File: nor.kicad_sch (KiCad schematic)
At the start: 4 parts, among them Q10 2N7002, Q11 DMP3099L, Q12 DMP3099L, Q9 2N7002

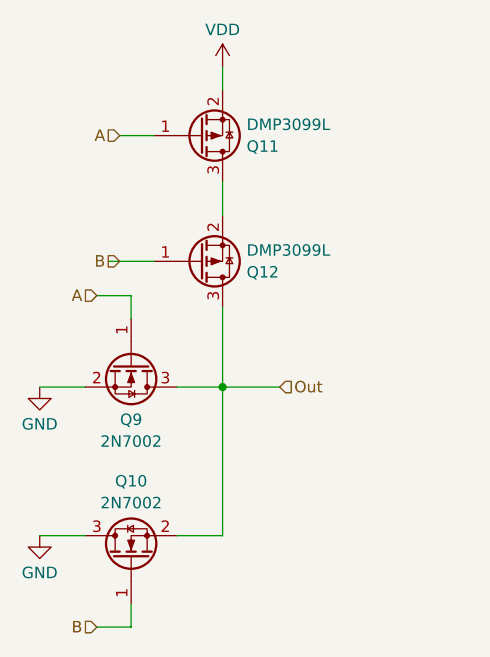
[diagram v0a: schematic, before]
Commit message: moved to 3v3
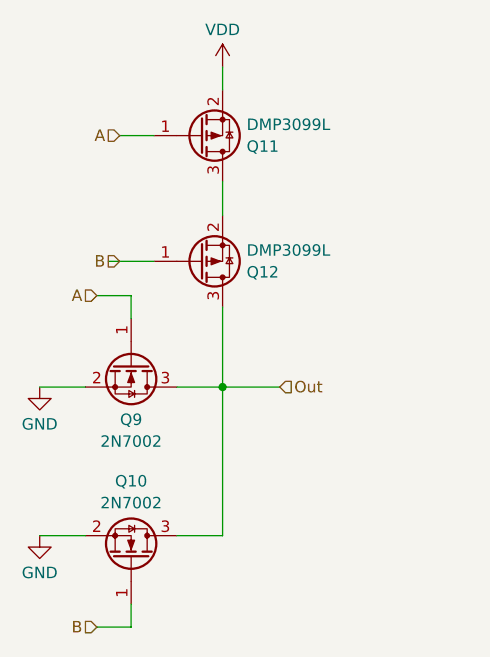
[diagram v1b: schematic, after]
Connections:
- net GND: now also Q10.2 (S); no longer Q10.3 (D)
- net Out: now also Q10.3 (D); no longer Q10.2 (S)
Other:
- moved on the sheet: Q10
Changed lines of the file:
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@@
 	(symbol
 		(lib_id "Transistor_FET:2N7002")
-		(at 106.68 109.22 90)
+		(at 106.68 109.22 270)
+		(mirror x)
 		(unit 1)
 		(exclude_from_sim no)
@@
 		(on_board yes)
 		(dnp no)
-		(fields_autoplaced yes)
 		(property "Reference" "Q10"
 			(at 106.68 100.6305 90)
@@
 		)
 		(property "Footprint" "Package_TO_SOT_SMD:SOT-23"
-			(at 108.585 104.14 0)
+			(at 104.775 104.14 0)
 			(effects
 				(font
@@
 		)
 		(property "Datasheet" "https://www.onsemi.com/pub/Collateral/NDS7002A-D.PDF"
-			(at 110.49 104.14 0)
+			(at 102.87 104.14 0)
 			(effects
 				(font

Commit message: added decoupling caps
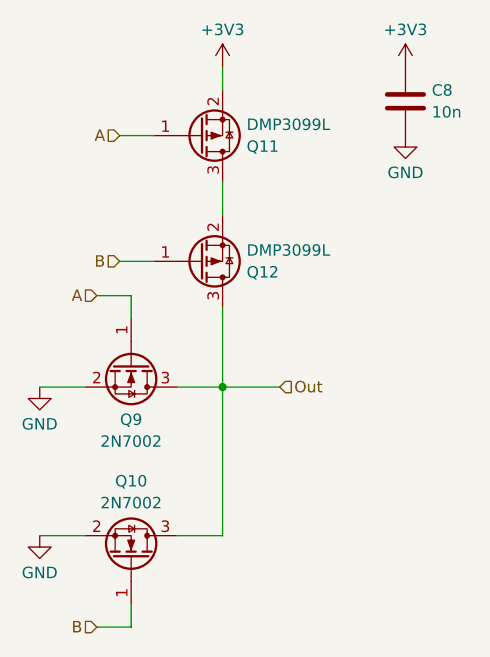
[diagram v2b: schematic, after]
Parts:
- added C8: 10n, symbol Device:C
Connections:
- net GND: now also C8.2
- net VDD renamed +3V3
- net +3V3: now also C8.1
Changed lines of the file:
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@@
 	(wire
 		(pts
-			(xy 104.14 76.2) (xy 109.22 76.2)
+			(xy 105.41 76.2) (xy 109.22 76.2)
 		)
 		(stroke
@@
 	)
 	(symbol
-		(lib_id "power:VDD")
-		(at 116.84 54.61 0)
+		(lib_id "power:GND")
+		(at 137.16 62.23 0)
 		(unit 1)
 		(exclude_from_sim no)
@@
 		(dnp no)
 		(fields_autoplaced yes)
-		(property "Reference" "#PWR011"
-			(at 116.84 58.42 0)
-			(effects
-				(font
-					(size 1.27 1.27)
-				)
-				(hide yes)
-			)
-		)
-		(property "Value" "VDD"
-			(at 116.84 50.4769 0)
+		(property "Reference" "#PWR0125"
+			(at 137.16 68.58 0)
+			(effects
+				(font
+					(size 1.27 1.27)
+				)
+				(hide yes)
+			)
+		)
+		(property "Value" "GND"
+			(at 137.16 66.3631 0)
 			(effects
 				(font
@@
 		)
 		(property "Footprint" ""
-			(at 116.84 54.61 0)
+			(at 137.16 62.23 0)
 			(effects
 				(font
@@
 		)
 		(property "Datasheet" ""
-			(at 116.84 54.61 0)
-			(effects
-				(font
-					(size 1.27 1.27)
-				)
-				(hide yes)
-			)
-		)
-		(property "Description" "Power symbol creates a global label with name \"VDD\""
-			(at 116.84 54.61 0)
+			(at 137.16 62.23 0)
+			(effects
+				(font
+					(size 1.27 1.27)
+				)
+				(hide yes)
+			)
+		)
+		(property "Description" "Power symbol creates a global label with name \"GND\" , ground"
+			(at 137.16 62.23 0)
 			(effects
 				(font
@@
 			(project "transistor-clock"
 				(path "/ce10d5bc-995e-4952-aa76-0a08f713a0f2/03f5a64c-acc7-49a6-878d-c157134676c1"
-					(reference "#PWR014")
-					(unit 1)
-				)
-				(path "/ce10d5bc-995e-4952-aa76-0a08f713a0f2/a0fc00b7-683e-4c06-a14c-1ec0a74c6be8"
-					(reference "#PWR011")
-					(unit 1)
-				)
-				(path "/ce10d5bc-995e-4952-aa76-0a08f713a0f2/f9206f2e-f283-4df4-91d8-f928dc25ba86"
-					(reference "#PWR017")
+					(reference "#PWR0446")
+					(unit 1)
+				)
+				(path "/ce10d5bc-995e-4952-aa76-0a08f713a0f2/a0fc00b7-683e-4c06-a14c-1ec0a74c6be8"
+					(reference "#PWR0125")
+					(unit 1)
+				)
+				(path "/ce10d5bc-995e-4952-aa76-0a08f713a0f2/f9206f2e-f283-4df4-91d8-f928dc25ba86"
+					(reference "#PWR0448")
 					(unit 1)
 				)
@@
 	)
 	(symbol
+		(lib_id "power:+3V3")
+		(at 116.84 54.61 0)
+		(unit 1)
+		(exclude_from_sim no)
+		(in_bom yes)
+		(on_board yes)
+		(dnp no)
+		(fields_autoplaced yes)
+		(property "Reference" "#PWR0322"
+			(at 116.84 58.42 0)
+			(effects
+				(font
+					(size 1.27 1.27)
+				)
+				(hide yes)
+			)
+		)
+		(property "Value" "+3V3"
+			(at 116.84 50.4769 0)
+			(effects
+				(font
+					(size 1.27 1.27)
+				)
+			)
+		)
+		(property "Footprint" ""
+			(at 116.84 54.61 0)
+			(effects
+				(font
+					(size 1.27 1.27)
+				)
+				(hide yes)
+			)
+		)
+		(property "Datasheet" ""
+			(at 116.84 54.61 0)
+			(effects
+				(font
+					(size 1.27 1.27)
+				)
+				(hide yes)
+			)
+		)
+		(property "Description" "Power symbol creates a global label with name \"+3V3\""
+			(at 116.84 54.61 0)
+			(effects
+				(font
+					(size 1.27 1.27)
+				)
+				(hide yes)
+			)
+		)
+		(pin "1"
+		)
+		(instances
+			(project ""
+				(path "/ce10d5bc-995e-4952-aa76-0a08f713a0f2/03f5a64c-acc7-49a6-878d-c157134676c1"
+					(reference "#PWR0324")
+					(unit 1)
+				)
+				(path "/ce10d5bc-995e-4952-aa76-0a08f713a0f2/a0fc00b7-683e-4c06-a14c-1ec0a74c6be8"
+					(reference "#PWR0322")
+					(unit 1)
+				)
+				(path "/ce10d5bc-995e-4952-aa76-0a08f713a0f2/f9206f2e-f283-4df4-91d8-f928dc25ba86"
+					(reference "#PWR0450")
+					(unit 1)
+				)
+			)
+		)
+	)
+	(symbol
 		(lib_id "Transistor_FET:2N7002")
 		(at 106.68 109.22 270)
@@
 	)
 	(symbol
+		(lib_id "power:+3V3")
+		(at 137.16 54.61 0)
+		(unit 1)
+		(exclude_from_sim no)
+		(in_bom yes)
+		(on_board yes)
+		(dnp no)
+		(fields_autoplaced yes)
+		(property "Reference" "#PWR011"
+			(at 137.16 58.42 0)
+			(effects
+				(font
+					(size 1.27 1.27)
+				)
+				(hide yes)
+			)
+		)
+		(property "Value" "+3V3"
+			(at 137.16 50.4769 0)
+			(effects
+				(font
+					(size 1.27 1.27)
+				)
+			)
+		)
+		(property "Footprint" ""
+			(at 137.16 54.61 0)
+			(effects
+				(font
+					(size 1.27 1.27)
+				)
+				(hide yes)
+			)
+		)
+		(property "Datasheet" ""
+			(at 137.16 54.61 0)
+			(effects
+				(font
+					(size 1.27 1.27)
+				)
+				(hide yes)
+			)
+		)
+		(property "Description" "Power symbol creates a global label with name \"+3V3\""
+			(at 137.16 54.61 0)
+			(effects
+				(font
+					(size 1.27 1.27)
+				)
+				(hide yes)
+			)
+		)
+		(pin "1"
+		)
+		(instances
+			(project "transistor-clock"
+				(path "/ce10d5bc-995e-4952-aa76-0a08f713a0f2/03f5a64c-acc7-49a6-878d-c157134676c1"
+					(reference "#PWR017")
+					(unit 1)
+				)
+				(path "/ce10d5bc-995e-4952-aa76-0a08f713a0f2/a0fc00b7-683e-4c06-a14c-1ec0a74c6be8"
+					(reference "#PWR011")
+					(unit 1)
+				)
+				(path "/ce10d5bc-995e-4952-aa76-0a08f713a0f2/f9206f2e-f283-4df4-91d8-f928dc25ba86"
+					(reference "#PWR0120")
+					(unit 1)
+				)
+			)
+		)
+	)
+	(symbol
 		(lib_id "power:GND")
 		(at 96.52 90.17 0)
@@
 					(unit 1)
 				)
+			)
+		)
+	)
+	(symbol
+		(lib_id "Device:C")
+		(at 137.16 58.42 0)
+		(unit 1)
+		(exclude_from_sim no)
+		(in_bom yes)
+		(on_board yes)
+		(dnp no)
+		(fields_autoplaced yes)
+		(property "Reference" "C8"
+			(at 140.081 57.2078 0)
+			(effects
+				(font
+					(size 1.27 1.27)
+				)
+				(justify left)
+			)
+		)
+		(property "Value" "10n"
+			(at 140.081 59.6321 0)
+			(effects
+				(font
+					(size 1.27 1.27)
+				)
+				(justify left)
+			)
+		)
+		(property "Footprint" ""
+			(at 138.1252 62.23 0)
+			(effects
+				(font
+					(size 1.27 1.27)
+				)
+				(hide yes)
+			)
+		)
+		(property "Datasheet" "~"
+			(at 137.16 58.42 0)
+			(effects
+				(font
+					(size 1.27 1.27)
+				)
+				(hide yes)
+			)
+		)
+		(property "Description" "Unpolarized capacitor"
+			(at 137.16 58.42 0)
+			(effects
+				(font
+					(size 1.27 1.27)
+				)
+				(hide yes)
+			)
+		)
+		(pin "2"
+		)
+		(pin "1"
+		)
+		(instances
+			(project ""
+				(path "/ce10d5bc-995e-4952-aa76-0a08f713a0f2/03f5a64c-acc7-49a6-878d-c157134676c1"
+					(reference "C10")
+					(unit 1)
+				)
+				(path "/ce10d5bc-995e-4952-aa76-0a08f713a0f2/a0fc00b7-683e-4c06-a14c-1ec0a74c6be8"
+					(reference "C8")
+					(unit 1)
+				)
+				(path "/ce10d5bc-995e-4952-aa76-0a08f713a0f2/f9206f2e-f283-4df4-91d8-f928dc25ba86"
+					(reference "C14")
+					(unit 1)
+				)

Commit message: corrected output/input type of pins
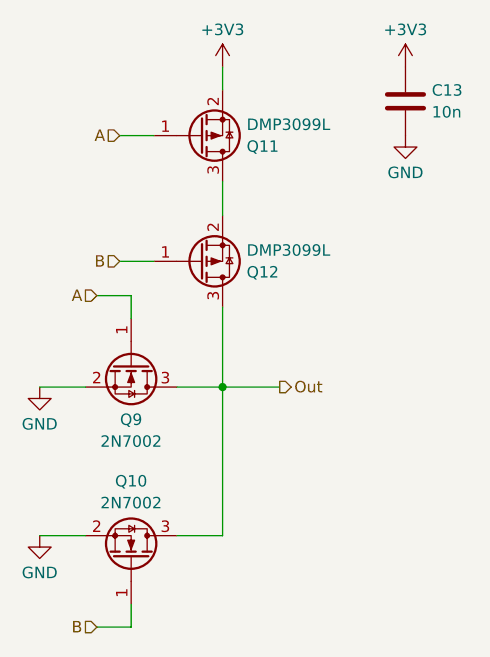
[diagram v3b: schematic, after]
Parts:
- C13: renamed from C8; footprint (none) -> Capacitor_SMD:C_0603_1608Metric
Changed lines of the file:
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@@
 	)
 	(hierarchical_label "Out"
-		(shape input)
+		(shape output)
 		(at 123.19 90.17 0)
 		(effects
@@
 		(dnp no)
 		(fields_autoplaced yes)
-		(property "Reference" "#PWR0125"
+		(property "Reference" "#PWR015"
 			(at 137.16 68.58 0)
 			(effects
@@
 			(project "transistor-clock"
 				(path "/ce10d5bc-995e-4952-aa76-0a08f713a0f2/03f5a64c-acc7-49a6-878d-c157134676c1"
-					(reference "#PWR0446")
-					(unit 1)
-				)
-				(path "/ce10d5bc-995e-4952-aa76-0a08f713a0f2/a0fc00b7-683e-4c06-a14c-1ec0a74c6be8"
-					(reference "#PWR0125")
-					(unit 1)
-				)
-				(path "/ce10d5bc-995e-4952-aa76-0a08f713a0f2/f9206f2e-f283-4df4-91d8-f928dc25ba86"
-					(reference "#PWR0448")
+					(reference "#PWR020")
+					(unit 1)
+				)
+				(path "/ce10d5bc-995e-4952-aa76-0a08f713a0f2/a0fc00b7-683e-4c06-a14c-1ec0a74c6be8"
+					(reference "#PWR015")
+					(unit 1)
+				)
+				(path "/ce10d5bc-995e-4952-aa76-0a08f713a0f2/f9206f2e-f283-4df4-91d8-f928dc25ba86"
+					(reference "#PWR025")
 					(unit 1)
 				)
@@
 		(dnp no)
 		(fields_autoplaced yes)
-		(property "Reference" "#PWR0322"
+		(property "Reference" "#PWR013"
 			(at 116.84 58.42 0)
 			(effects
@@
 			(project ""
 				(path "/ce10d5bc-995e-4952-aa76-0a08f713a0f2/03f5a64c-acc7-49a6-878d-c157134676c1"
-					(reference "#PWR0324")
-					(unit 1)
-				)
-				(path "/ce10d5bc-995e-4952-aa76-0a08f713a0f2/a0fc00b7-683e-4c06-a14c-1ec0a74c6be8"
-					(reference "#PWR0322")
-					(unit 1)
-				)
-				(path "/ce10d5bc-995e-4952-aa76-0a08f713a0f2/f9206f2e-f283-4df4-91d8-f928dc25ba86"
-					(reference "#PWR0450")
+					(reference "#PWR018")
+					(unit 1)
+				)
+				(path "/ce10d5bc-995e-4952-aa76-0a08f713a0f2/a0fc00b7-683e-4c06-a14c-1ec0a74c6be8"
+					(reference "#PWR013")
+					(unit 1)
+				)
+				(path "/ce10d5bc-995e-4952-aa76-0a08f713a0f2/f9206f2e-f283-4df4-91d8-f928dc25ba86"
+					(reference "#PWR023")
 					(unit 1)
 				)
@@
 		(dnp no)
 		(fields_autoplaced yes)
-		(property "Reference" "#PWR011"
+		(property "Reference" "#PWR014"
 			(at 137.16 58.42 0)
 			(effects
@@
 			(project "transistor-clock"
 				(path "/ce10d5bc-995e-4952-aa76-0a08f713a0f2/03f5a64c-acc7-49a6-878d-c157134676c1"
-					(reference "#PWR017")
-					(unit 1)
-				)
-				(path "/ce10d5bc-995e-4952-aa76-0a08f713a0f2/a0fc00b7-683e-4c06-a14c-1ec0a74c6be8"
-					(reference "#PWR011")
-					(unit 1)
-				)
-				(path "/ce10d5bc-995e-4952-aa76-0a08f713a0f2/f9206f2e-f283-4df4-91d8-f928dc25ba86"
-					(reference "#PWR0120")
+					(reference "#PWR019")
+					(unit 1)
+				)
+				(path "/ce10d5bc-995e-4952-aa76-0a08f713a0f2/a0fc00b7-683e-4c06-a14c-1ec0a74c6be8"
+					(reference "#PWR014")
+					(unit 1)
+				)
+				(path "/ce10d5bc-995e-4952-aa76-0a08f713a0f2/f9206f2e-f283-4df4-91d8-f928dc25ba86"
+					(reference "#PWR024")
 					(unit 1)
 				)
@@
 		(dnp no)
 		(fields_autoplaced yes)
-		(property "Reference" "#PWR09"
+		(property "Reference" "#PWR011"
 			(at 96.52 96.52 0)
 			(effects
@@
 			(project "transistor-clock"
 				(path "/ce10d5bc-995e-4952-aa76-0a08f713a0f2/03f5a64c-acc7-49a6-878d-c157134676c1"
-					(reference "#PWR012")
-					(unit 1)
-				)
-				(path "/ce10d5bc-995e-4952-aa76-0a08f713a0f2/a0fc00b7-683e-4c06-a14c-1ec0a74c6be8"
-					(reference "#PWR09")
-					(unit 1)
-				)
-				(path "/ce10d5bc-995e-4952-aa76-0a08f713a0f2/f9206f2e-f283-4df4-91d8-f928dc25ba86"
-					(reference "#PWR015")
+					(reference "#PWR016")
+					(unit 1)
+				)
+				(path "/ce10d5bc-995e-4952-aa76-0a08f713a0f2/a0fc00b7-683e-4c06-a14c-1ec0a74c6be8"
+					(reference "#PWR011")
+					(unit 1)
+				)
+				(path "/ce10d5bc-995e-4952-aa76-0a08f713a0f2/f9206f2e-f283-4df4-91d8-f928dc25ba86"
+					(reference "#PWR021")
 					(unit 1)
 				)
@@
 		(dnp no)
 		(fields_autoplaced yes)
-		(property "Reference" "#PWR010"
+		(property "Reference" "#PWR012"
 			(at 96.52 113.03 0)
 			(effects
@@
 			(project "transistor-clock"
 				(path "/ce10d5bc-995e-4952-aa76-0a08f713a0f2/03f5a64c-acc7-49a6-878d-c157134676c1"
-					(reference "#PWR013")
-					(unit 1)
-				)
-				(path "/ce10d5bc-995e-4952-aa76-0a08f713a0f2/a0fc00b7-683e-4c06-a14c-1ec0a74c6be8"
-					(reference "#PWR010")
-					(unit 1)
-				)
-				(path "/ce10d5bc-995e-4952-aa76-0a08f713a0f2/f9206f2e-f283-4df4-91d8-f928dc25ba86"
-					(reference "#PWR016")
+					(reference "#PWR017")
+					(unit 1)
+				)
+				(path "/ce10d5bc-995e-4952-aa76-0a08f713a0f2/a0fc00b7-683e-4c06-a14c-1ec0a74c6be8"
+					(reference "#PWR012")
+					(unit 1)
+				)
+				(path "/ce10d5bc-995e-4952-aa76-0a08f713a0f2/f9206f2e-f283-4df4-91d8-f928dc25ba86"
+					(reference "#PWR022")
 					(unit 1)
 				)
@@
 		(dnp no)
 		(fields_autoplaced yes)
-		(property "Reference" "C8"
+		(property "Reference" "C13"
 			(at 140.081 57.2078 0)
 			(effects
@@
 			)
 		)
-		(property "Footprint" ""
+		(property "Footprint" "Capacitor_SMD:C_0603_1608Metric"
 			(at 138.1252 62.23 0)
 			(effects
@@
 			(project ""
 				(path "/ce10d5bc-995e-4952-aa76-0a08f713a0f2/03f5a64c-acc7-49a6-878d-c157134676c1"
-					(reference "C10")
-					(unit 1)
-				)
-				(path "/ce10d5bc-995e-4952-aa76-0a08f713a0f2/a0fc00b7-683e-4c06-a14c-1ec0a74c6be8"
-					(reference "C8")
-					(unit 1)
-				)
-				(path "/ce10d5bc-995e-4952-aa76-0a08f713a0f2/f9206f2e-f283-4df4-91d8-f928dc25ba86"
 					(reference "C14")
 					(unit 1)
 				)
+				(path "/ce10d5bc-995e-4952-aa76-0a08f713a0f2/a0fc00b7-683e-4c06-a14c-1ec0a74c6be8"
+					(reference "C13")
+					(unit 1)
+				)
+				(path "/ce10d5bc-995e-4952-aa76-0a08f713a0f2/f9206f2e-f283-4df4-91d8-f928dc25ba86"
+					(reference "C15")
+					(unit 1)
+				)
